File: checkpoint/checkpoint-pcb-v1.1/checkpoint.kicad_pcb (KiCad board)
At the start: 4 copper layers, 85.2 x 39.6 mm, 111 parts, among them J1 T0, J10 CAN_OUT, J11 BOOT, J12 Y_ENDSTOP, J13 SERVO, J14 RGB, J15 SWD, J16 USB_C_Receptacle_USB2.0_16P, J17 PWR_CAN_IN, J18 PWR_OUT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

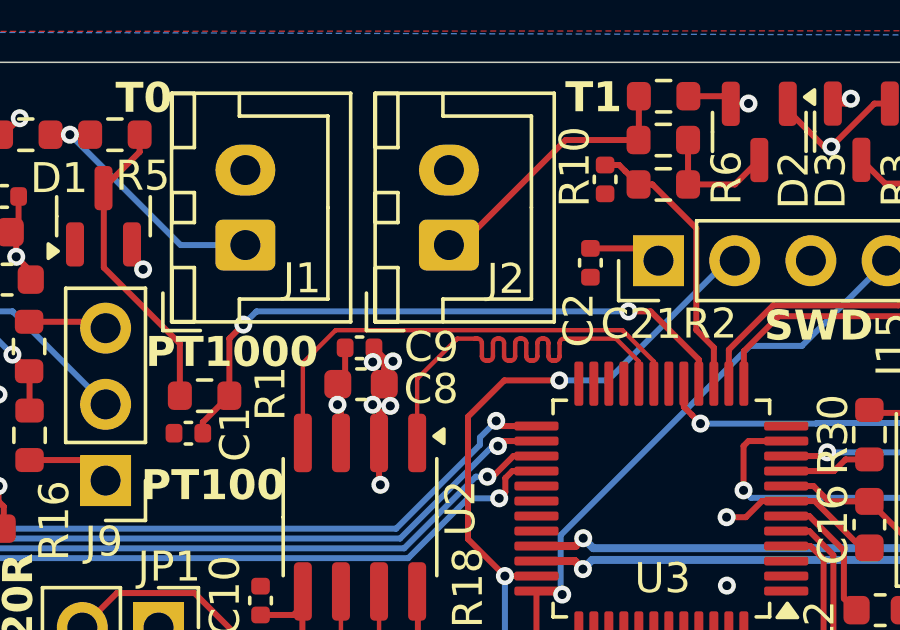
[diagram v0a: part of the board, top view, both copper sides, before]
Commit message: chore: remove 3.3v trace overlapping 3.3v zone
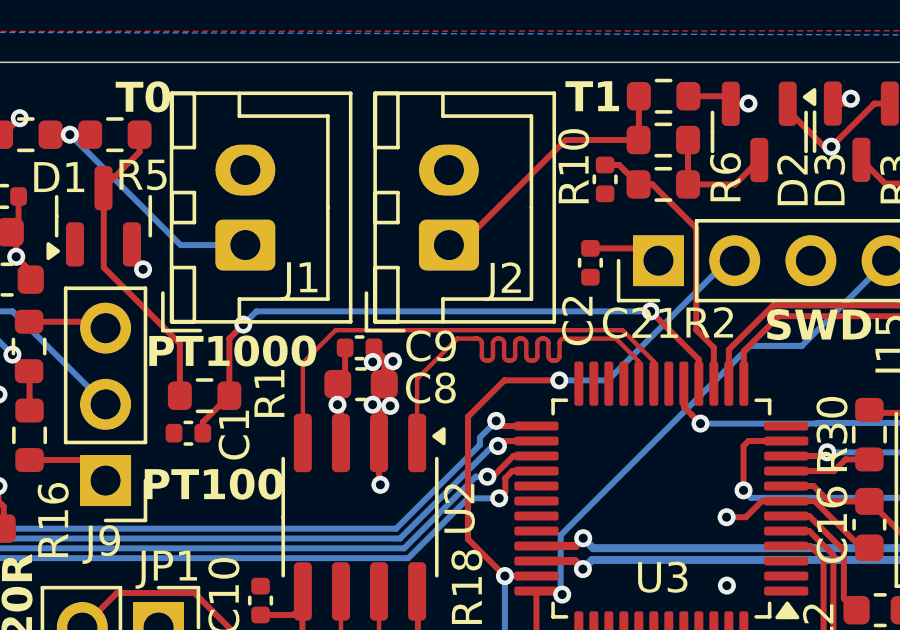
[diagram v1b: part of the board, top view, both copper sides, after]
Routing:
- net +3.3V: track 117.7 -> 110.3 mm
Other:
- board text added: "CANBUS Checkpoint ${REVISION}"
- board text removed: "CAN bus Checkpoint ${REVISION}"
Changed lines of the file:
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@@
 		)
 	)
-	(gr_text "CAN bus Checkpoint ${REVISION}"
+	(gr_text "CANBUS Checkpoint ${REVISION}"
 		(at 77.080408 68.951118 0)
 		(layer "B.SilkS")
@@
 	)
 	(segment
+		(start 47.2 46.056526)
+		(end 48.085408 45.171118)
+		(width 0.2)
+		(layer "F.Cu")
+		(net 1)
+	)
+	(segment
+		(start 48.550408 42.801118)
+		(end 48.085408 43.266118)
+		(width 0.2)
+		(layer "F.Cu")
+		(net 1)
+	)
+	(segment
 		(start 62.130408 42.361118)
 		(end 63.735 43.96571)
@@
 	)
 	(segment
-		(start 47.2 46.056526)
-		(end 48.085408 45.171118)
-		(width 0.2)
-		(layer "F.Cu")
-		(net 1)
-	)
-	(segment
-		(start 48.550408 42.801118)
-		(end 48.085408 43.266118)
-		(width 0.2)
-		(layer "F.Cu")
-		(net 1)
-	)
-	(segment
-		(start 61.390408 42.361118)
-		(end 62.130408 42.361118)
-		(width 0.2)
-		(layer "F.Cu")
-		(net 1)
-	)
-	(segment
 		(start 63.735 43.96571)
 		(end 63.735 44.77)
@@
 	)
 	(via
-		(at 61.390408 42.361118)
+		(at 62.130408 42.361118)
 		(size 0.6)
 		(drill 0.3)
@@
 	)
 	(segment
-		(start 48.990408 42.361118)
-		(end 61.390408 42.361118)
+		(start 62.130408 42.361118)
+		(end 48.990408 42.361118)
 		(width 0.2)
 		(layer "B.Cu")
@@
 	)
 	(segment
-		(start 48.550408 42.801118)
-		(end 48.990408 42.361118)
+		(start 48.990408 42.361118)
+		(end 48.550408 42.801118)
 		(width 0.2)
 		(layer "B.Cu")
@@
 	)
 	(segment
-		(start 62.390408 43.161118)
-		(end 62.390408 40.671118)
-		(width 1)
-		(layer "In1.Cu")
-		(net 6)
-	)
-	(segment
 		(start 35.71 48.301118)
 		(end 33.65 50.361118)
@@
 	)
 	(segment
+		(start 68.3 56.32)
+		(end 69.740408 54.879592)
+		(width 1)
+		(layer "In1.Cu")
+		(net 6)
+	)
+	(segment
 		(start 80.775408 59.896118)
 		(end 85.000408 64.121118)
@@
 	)
 	(segment
-		(start 68.3 56.32)
-		(end 68.3 49.07071)
+		(start 69.740408 54.879592)
+		(end 69.740408 46.161118)
 		(width 1)
 		(layer "In1.Cu")
@@
 		(layer "In1.Cu")
 		(net 6)
-	)
-	(segment
-		(start 68.3 49.07071)
-		(end 62.390408 43.161118)
-		(width 1)
-		(layer "In1.Cu")
-		(net 6)

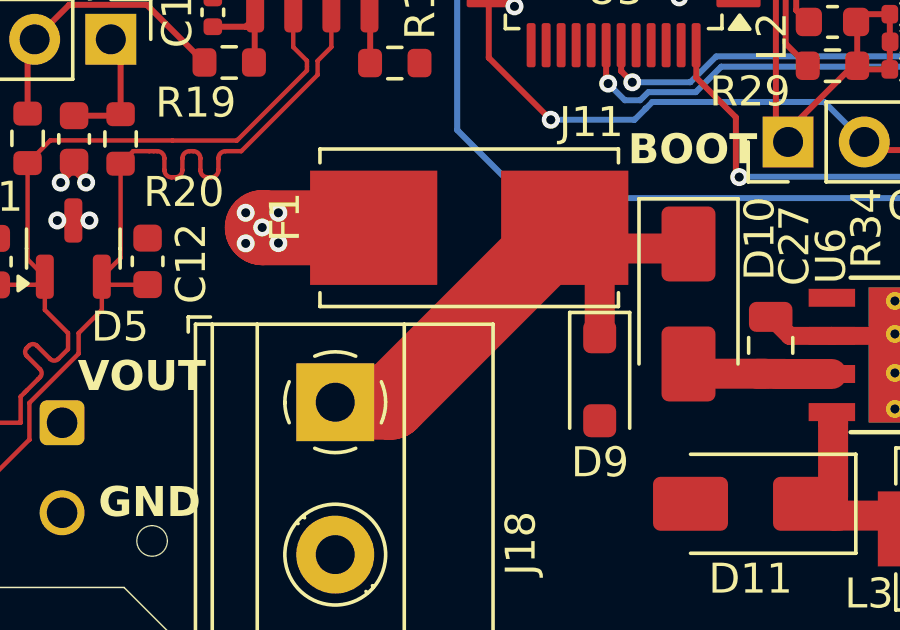
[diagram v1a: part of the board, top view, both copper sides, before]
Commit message: chore: make some space between fused vin/vout traces
chore: cleanup traces
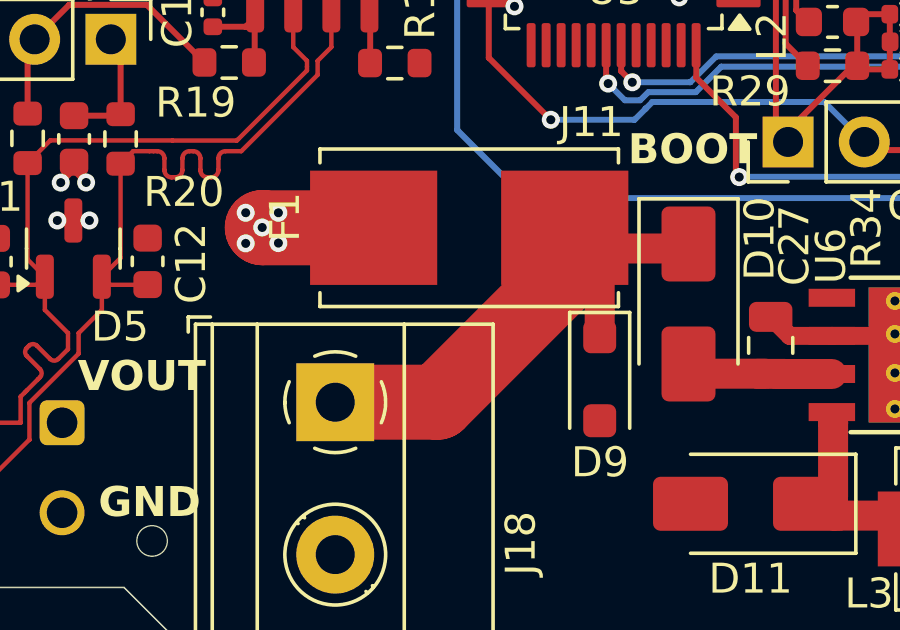
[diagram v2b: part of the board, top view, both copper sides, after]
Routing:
- net VOUT: track 16.0 -> 16.9 mm
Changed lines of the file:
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@@
 	)
 	(segment
-		(start 55.040408 64.996118)
-		(end 60.855408 59.181118)
+		(start 53.205408 64.996118)
+		(end 56.615408 64.996118)
 		(width 2.5)
 		(layer "F.Cu")
@@
 	)
 	(segment
+		(start 56.615408 64.996118)
+		(end 60.855408 60.756118)
+		(width 2.5)
+		(layer "F.Cu")
+		(net 92)
+	)
+	(segment
 		(start 65.022908 59.871118)
 		(end 61.595408 59.871118)
@@
 	)
 	(segment
-		(start 53.205408 64.996118)
-		(end 55.040408 64.996118)
+		(start 60.855408 60.756118)
+		(end 60.855408 59.181118)
 		(width 2.5)
 		(layer "F.Cu")
